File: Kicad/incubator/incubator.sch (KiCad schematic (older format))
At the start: 25 parts, among them J1 Barrel_Jack_MountingPin, J2 Conn_01x06, J3 Conn_01x01, J4 RJ12, J5 Conn_01x01, J6 Conn_01x01, J7 Conn_01x01, J8 Conn_02x03_Odd_Even, U1 LM78M05_TO252

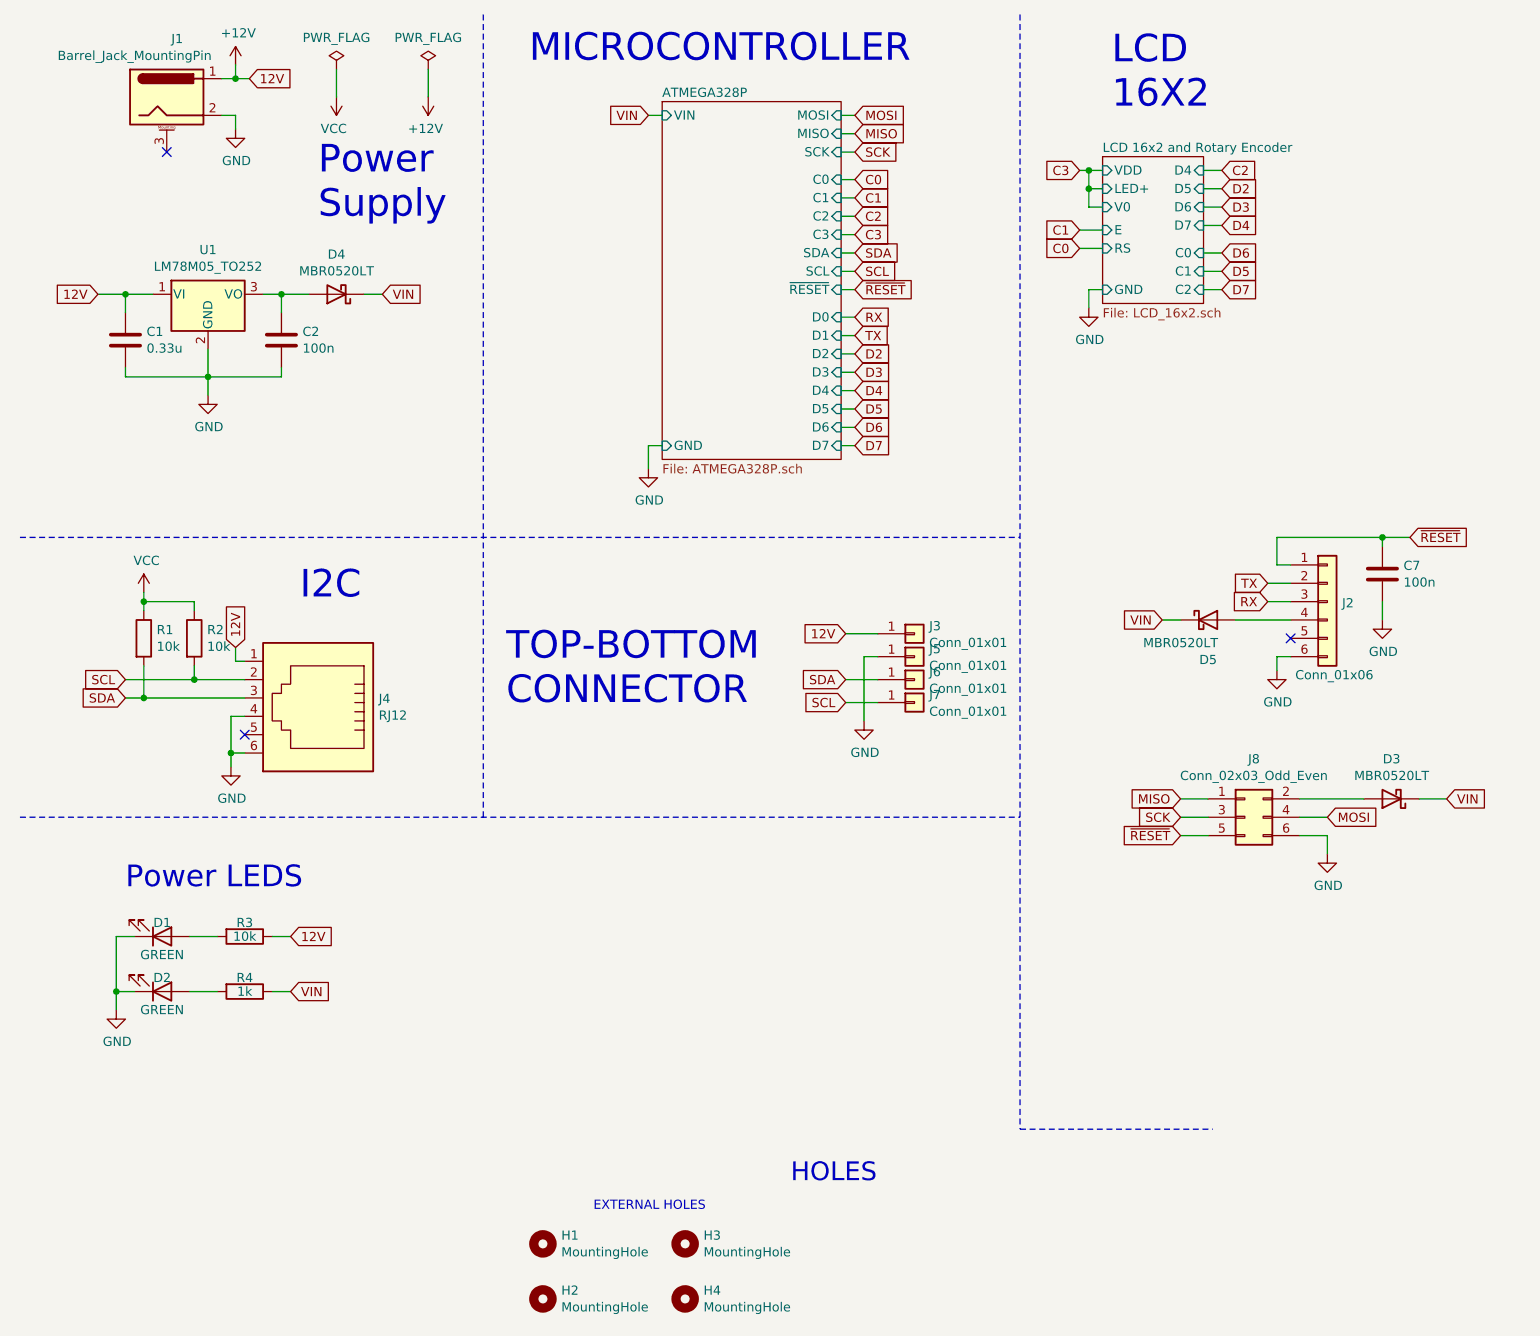
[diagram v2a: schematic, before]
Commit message: fix: iss #1: add ERROR and BLINKING LED, iss #2: solved
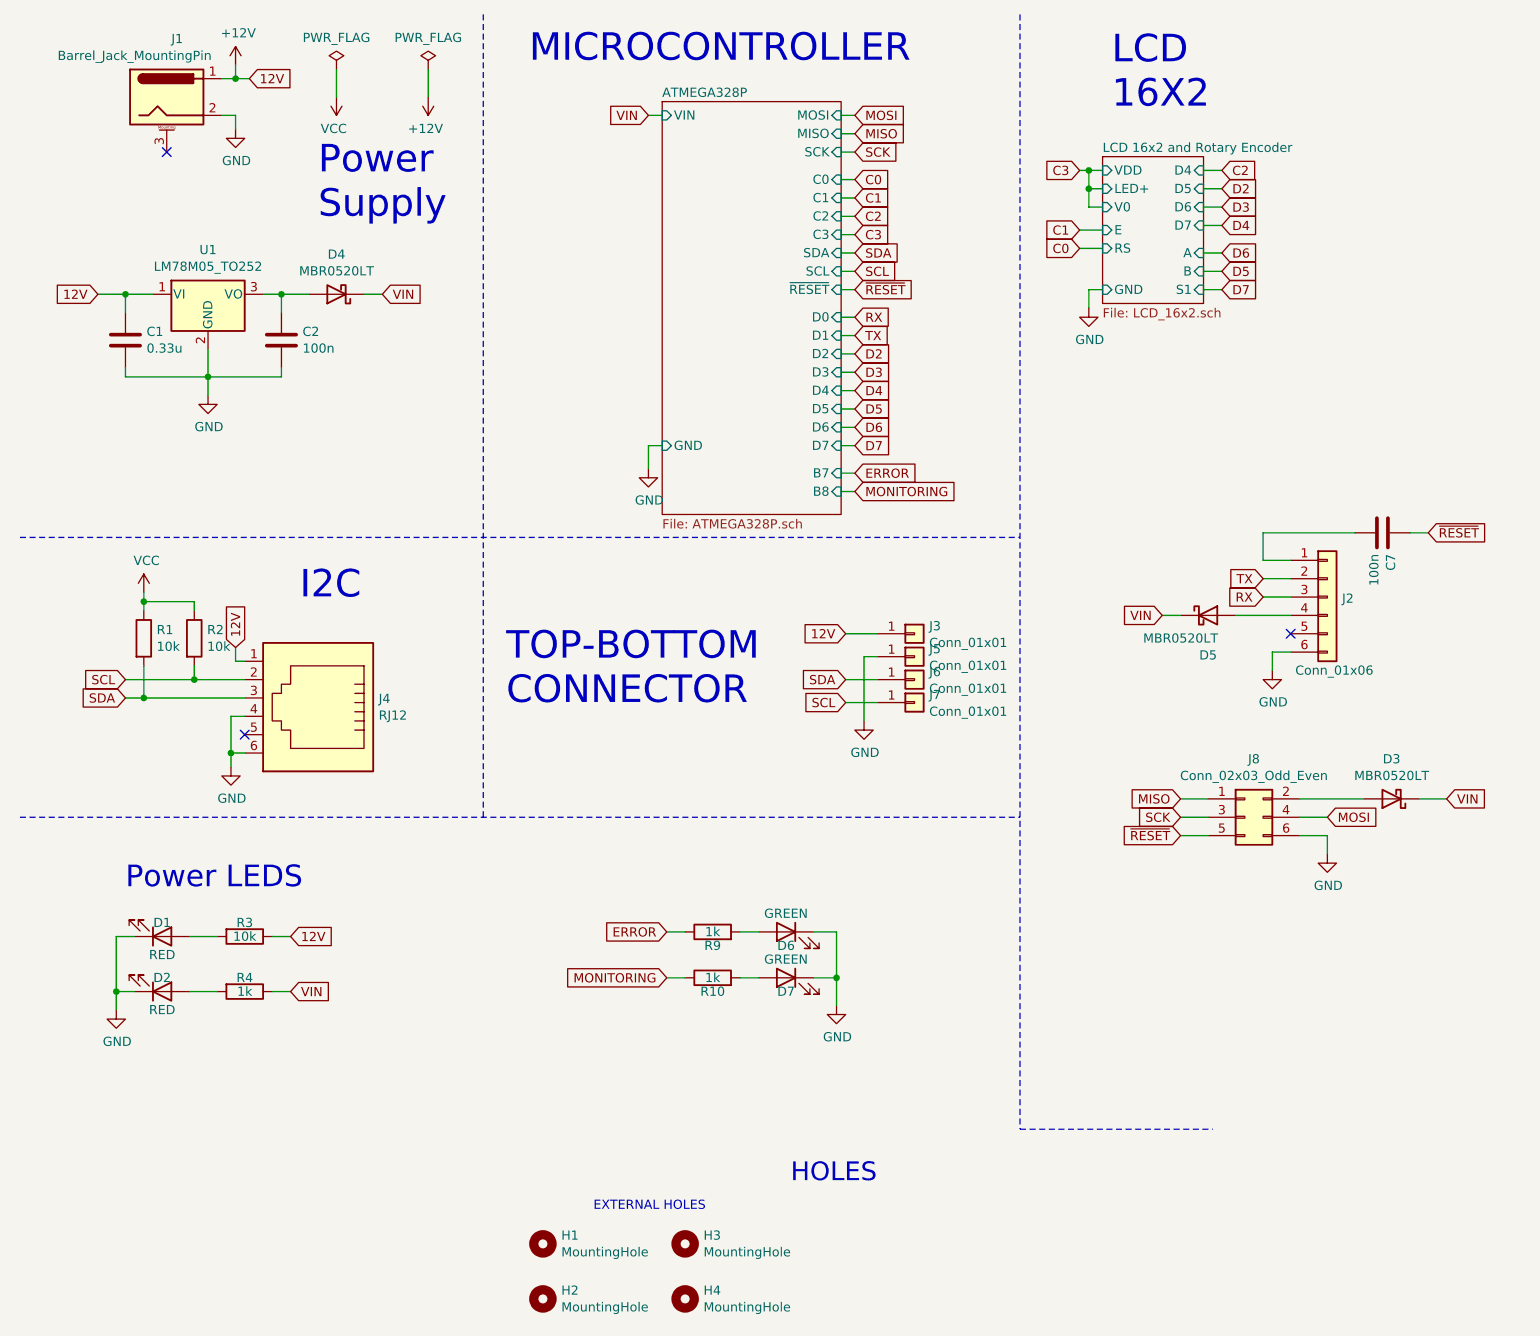
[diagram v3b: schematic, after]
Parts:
- added D6, D7: GREEN, LED_SMD:LED_0805_2012Metric_Pad1.15x1.40mm_HandSolder, symbol Device:LED
- added R10, R9: 1k, Resistor_SMD:R_0805_2012Metric_Pad1.20x1.40mm_HandSolder, symbol Device:R
- D1, D2: value GREEN -> RED
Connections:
- net GND: now also D6.1 (K), D7.1 (K); no longer C7.2
- net ~RESET: no longer J2.1 (Pin_1)
- new net: C7.2, J2.1 (Pin_1)
- new net: D7.2 (A), R10.2
- new net: D6.2 (A), R9.2
- new net ERROR: R9.1
- new net MONITORING: R10.1
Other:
- moved on the sheet: C7, D5, J2
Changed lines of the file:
@@
 Title "Incubator"
 Date "2021-07-26"
-Rev "0.1"
+Rev "0.2"
 Comp ""
 Comment1 ""
@@
 $EndComp
 $Sheet
-S 3975 950  975  1950
+S 3975 950  975  2250
 U 61116939
 F0 "ATMEGA328P" 50
@@
 F20 "MISO" I R 4950 1125 50
 F21 "SCK" I R 4950 1225 50
+F22 "B7" I R 4950 2975 50
+F23 "B8" I R 4950 3075 50
 $EndSheet
 Wire Wire Line
@@
 Wire Wire Line
 	3900 2825 3900 2950
-Text GLabel 6250 1325 0    50   Input ~ 0
-C3
-Text GLabel 6250 1650 0    50   Input ~ 0
-C1
-Text GLabel 6250 1750 0    50   Input ~ 0
-C0
-Text GLabel 7025 1325 2    50   Input ~ 0
-C2
-Text GLabel 7025 1425 2    50   Input ~ 0
-D2
-Text GLabel 7025 1525 2    50   Input ~ 0
-D3
-Text GLabel 7025 1625 2    50   Input ~ 0
-D4
-Text GLabel 7025 1775 2    50   Input ~ 0
-D6
-Text GLabel 7025 1875 2    50   Input ~ 0
-D5
-Text GLabel 7025 1975 2    50   Input ~ 0
-D7
 $Comp
 L incubator-rescue:GND-power #PWR0114
@@
 Wire Wire Line
 	6925 1525 7025 1525
-$Sheet
-S 6375 1250 550  800
-U 611AEB1E
-F0 "LCD 16x2 and Rotary Encoder" 50
-F1 "LCD_16x2.sch" 50
-F2 "D4" I R 6925 1325 50
-F3 "D5" I R 6925 1425 50
-F4 "D6" I R 6925 1525 50
-F5 "D7" I R 6925 1625 50
-F6 "GND" I L 6375 1975 50
-F7 "C0" I R 6925 1775 50
-F8 "C1" I R 6925 1875 50
-F9 "C2" I R 6925 1975 50
-F10 "E" I L 6375 1650 50
-F11 "RS" I L 6375 1750 50
-F12 "VDD" I L 6375 1325 50
-F13 "LED+" I L 6375 1425 50
-F14 "V0" I L 6375 1525 50
-$EndSheet
 Wire Wire Line
 	6925 1775 7025 1775
@@
 	1    0    0    -1
 $EndComp
-$Comp
-L incubator-rescue:Conn_01x06-Connector_Generic J2
-U 1 1 610D151B
-P 7600 3675
-F 0 "J2" H 7680 3667 50  0000 L CNN
-F 1 "Conn_01x06" H 7425 3275 50  0000 L CNN
-F 2 "Connector_PinHeader_2.54mm:PinHeader_1x06_P2.54mm_Vertical" H 7600 3675 50  0001 C CNN
-F 3 "~" H 7600 3675 50  0001 C CNN
-	1    7600 3675
-	1    0    0    -1
-$EndComp
 Text GLabel 2450 2000 2    50   Input ~ 0
 VIN
-Text GLabel 8050 3325 2    50   Input ~ 0
+Text GLabel 8150 3300 2    50   Input ~ 0
 ~RESET
-Text GLabel 7275 3575 0    50   Input ~ 0
+Text GLabel 7250 3550 0    50   Input ~ 0
 TX
 $Comp
 L incubator-rescue:GND-power #PWR0103
 U 1 1 610EBE3F
-P 7325 4050
-F 0 "#PWR0103" H 7325 3800 50  0001 C CNN
-F 1 "GND" H 7330 3877 50  0000 C CNN
-F 2 "" H 7325 4050 50  0001 C CNN
-F 3 "" H 7325 4050 50  0001 C CNN
-	1    7325 4050
-	1    0    0    -1
-$EndComp
-Wire Wire Line
-	7400 3575 7275 3575
-Wire Wire Line
-	7275 3675 7400 3675
-Wire Wire Line
-	7400 3975 7325 3975
-Wire Wire Line
-	7325 3975 7325 4050
-Text GLabel 7275 3675 0    50   Input ~ 0
+P 7300 4050
+F 0 "#PWR0103" H 7300 3800 50  0001 C CNN
+F 1 "GND" H 7305 3877 50  0000 C CNN
+F 2 "" H 7300 4050 50  0001 C CNN
+F 3 "" H 7300 4050 50  0001 C CNN
+	1    7300 4050
+	1    0    0    -1
+$EndComp
+Text GLabel 7250 3650 0    50   Input ~ 0
 RX
 $Comp
@@
 L incubator-rescue:C-Device C?
 U 1 1 61154027
-P 7900 3525
+P 7900 3300
 AR Path="/61116939/61154027" Ref="C?"  Part="1"
 AR Path="/61154027" Ref="C7"  Part="1"
-F 0 "C7" H 8015 3571 50  0000 L CNN
-F 1 "100n" H 8015 3480 50  0000 L CNN
-F 2 "Capacitor_SMD:C_0805_2012Metric_Pad1.18x1.45mm_HandSolder" H 7938 3375 50  0001 C CNN
-F 3 "~" H 7900 3525 50  0001 C CNN
-	1    7900 3525
-	1    0    0    -1
-$EndComp
-Wire Wire Line
-	7100 3775 7400 3775
-Wire Wire Line
-	6800 3775 6700 3775
-Text GLabel 6700 3775 0    50   Input ~ 0
+F 0 "C7" H 8015 3346 50  0000 L CNN
+F 1 "100n" H 8015 3255 50  0000 L CNN
+F 2 "Capacitor_SMD:C_0805_2012Metric_Pad1.18x1.45mm_HandSolder" H 7938 3150 50  0001 C CNN
+F 3 "~" H 7900 3300 50  0001 C CNN
+	1    7900 3300
+	0    1    1    0
+$EndComp
+Text GLabel 6700 3750 0    50   Input ~ 0
 VIN
-Wire Wire Line
-	7400 3475 7325 3475
-Wire Wire Line
-	7325 3475 7325 3325
-Wire Wire Line
-	7325 3325 7900 3325
-$Comp
-L incubator-rescue:GND-power #PWR0106
-U 1 1 6117A969
-P 7900 3775
-F 0 "#PWR0106" H 7900 3525 50  0001 C CNN
-F 1 "GND" H 7905 3602 50  0000 C CNN
-F 2 "" H 7900 3775 50  0001 C CNN
-F 3 "" H 7900 3775 50  0001 C CNN
-	1    7900 3775
-	1    0    0    -1
-$EndComp
-Wire Wire Line
-	7900 3775 7900 3675
-Wire Wire Line
-	7900 3375 7900 3325
-Connection ~ 7900 3325
-Wire Wire Line
-	7900 3325 8050 3325
 Text GLabel 1725 825  2    50   Input ~ 0
 12V
@@
 L incubator-rescue:MBR0520LT-Diode D5
 U 1 1 61109529
-P 6950 3775
-F 0 "D5" H 6950 3558 50  0000 C CNN
-F 1 "MBR0520LT" H 6800 3650 50  0000 C CNN
-F 2 "Diode_SMD:D_SOD-123" H 6950 3600 50  0001 C CNN
-F 3 "http://www.onsemi.com/pub_link/Collateral/MBR0520LT1-D.PDF" H 6950 3775 50  0001 C CNN
-	1    6950 3775
-	1    0    0    -1
-$EndComp
-NoConn ~ 7400 3875
+P 6950 3750
+F 0 "D5" H 6950 3533 50  0000 C CNN
+F 1 "MBR0520LT" H 6800 3625 50  0000 C CNN
+F 2 "Diode_SMD:D_SOD-123" H 6950 3575 50  0001 C CNN
+F 3 "http://www.onsemi.com/pub_link/Collateral/MBR0520LT1-D.PDF" H 6950 3750 50  0001 C CNN
+	1    6950 3750
+	1    0    0    -1
+$EndComp
 $Comp
 L incubator-rescue:Conn_01x01-Connector_Generic J3
@@
 AR Path="/614D57B2" Ref="D1"  Part="1"
 F 0 "D1" H 1250 5425 50  0000 C CNN
-F 1 "GREEN" H 1250 5600 50  0000 C CNN
+F 1 "RED" H 1250 5600 50  0000 C CNN
 F 2 "LED_SMD:LED_0805_2012Metric_Pad1.15x1.40mm_HandSolder" H 1250 5500 50  0001 C CNN
 F 3 "~" H 1250 5500 50  0001 C CNN
@@
 AR Path="/614D57B8" Ref="D2"  Part="1"
 F 0 "D2" H 1250 5725 50  0000 C CNN
-F 1 "GREEN" H 1250 5900 50  0000 C CNN
+F 1 "RED" H 1250 5900 50  0000 C CNN
 F 2 "LED_SMD:LED_0805_2012Metric_Pad1.15x1.40mm_HandSolder" H 1250 5800 50  0001 C CNN
 F 3 "~" H 1250 5800 50  0001 C CNN
@@
 Wire Wire Line
 	6800 4950 6950 4950
+$Comp
+L incubator-rescue:Conn_01x06-Connector_Generic J2
+U 1 1 610D151B
+P 7600 3650
+F 0 "J2" H 7680 3642 50  0000 L CNN
+F 1 "Conn_01x06" H 7425 3250 50  0000 L CNN
+F 2 "Connector_PinHeader_2.54mm:PinHeader_1x06_P2.54mm_Vertical" H 7600 3650 50  0001 C CNN
+F 3 "~" H 7600 3650 50  0001 C CNN
+	1    7600 3650
+	1    0    0    -1
+$EndComp
+Wire Wire Line
+	7750 3300 7250 3300
+Wire Wire Line
+	7250 3300 7250 3450
+Wire Wire Line
+	7250 3450 7400 3450
+Wire Wire Line
+	8050 3300 8150 3300
+Wire Wire Line
+	6700 3750 6800 3750
+Wire Wire Line
+	7100 3750 7400 3750
+NoConn ~ 7400 3850
+Wire Wire Line
+	7400 3950 7300 3950
+Wire Wire Line
+	7300 3950 7300 4050
+Wire Wire Line
+	7250 3650 7400 3650
+Wire Wire Line
+	7400 3550 7250 3550
+Text GLabel 6250 1750 0    50   Input ~ 0
+C0
+Text GLabel 6250 1650 0    50   Input ~ 0
+C1
+Text GLabel 6250 1325 0    50   Input ~ 0
+C3
+Text GLabel 7025 1625 2    50   Input ~ 0
+D4
+Text GLabel 7025 1525 2    50   Input ~ 0
+D3
+Text GLabel 7025 1425 2    50   Input ~ 0
+D2
+Text GLabel 7025 1325 2    50   Input ~ 0
+C2
+Text GLabel 7025 1975 2    50   Input ~ 0
+D7
+Text GLabel 7025 1875 2    50   Input ~ 0
+D5
+Text GLabel 7025 1775 2    50   Input ~ 0
+D6
+$Sheet
+S 6375 1250 550  800
+U 611AEB1E
+F0 "LCD 16x2 and Rotary Encoder" 50
+F1 "LCD_16x2.sch" 50
+F2 "D4" I R 6925 1325 50
+F3 "D5" I R 6925 1425 50
+F4 "D6" I R 6925 1525 50
+F5 "D7" I R 6925 1625 50
+F6 "GND" I L 6375 1975 50
+F7 "A" I R 6925 1775 50
+F8 "B" I R 6925 1875 50
+F9 "S1" I R 6925 1975 50
+F10 "E" I L 6375 1650 50
+F11 "RS" I L 6375 1750 50
+F12 "VDD" I L 6375 1325 50
+F13 "LED+" I L 6375 1425 50
+F14 "V0" I L 6375 1525 50
+$EndSheet
+$Comp
+L Device:R R?
+U 1 1 6193BEE6
+P 4250 5725
+AR Path="/5E0D7B92/6193BEE6" Ref="R?"  Part="1"
+AR Path="/5E0D7D04/6193BEE6" Ref="R?"  Part="1"
+AR Path="/6193BEE6" Ref="R10"  Part="1"
+AR Path="/5E0005EE/6193BEE6" Ref="R?"  Part="1"
+AR Path="/614262A1/6193BEE6" Ref="R?"  Part="1"
+F 0 "R10" V 4175 5725 50  0000 C CNN
+F 1 "1k" V 4250 5725 50  0000 C CNN
+F 2 "Resistor_SMD:R_0805_2012Metric_Pad1.20x1.40mm_HandSolder" V 4180 5725 50  0001 C CNN
+F 3 "~" H 4250 5725 50  0001 C CNN
+	1    4250 5725
+	0    -1   -1   0
+$EndComp
+$Comp
+L Device:LED D?
+U 1 1 6193C98D
+P 4650 5725
+AR Path="/614262A1/6193C98D" Ref="D?"  Part="1"
+AR Path="/6193C98D" Ref="D7"  Part="1"
+F 0 "D7" H 4650 5650 50  0000 C CNN
+F 1 "GREEN" H 4650 5825 50  0000 C CNN
+F 2 "LED_SMD:LED_0805_2012Metric_Pad1.15x1.40mm_HandSolder" H 4650 5725 50  0001 C CNN
+F 3 "~" H 4650 5725 50  0001 C CNN
+	1    4650 5725
+	-1   0    0    -1
+$EndComp
+$Comp
+L Device:R R?
+U 1 1 6193CDAE
+P 4250 5475
+AR Path="/5E0D7B92/6193CDAE" Ref="R?"  Part="1"
+AR Path="/5E0D7D04/6193CDAE" Ref="R?"  Part="1"
+AR Path="/6193CDAE" Ref="R9"  Part="1"
+AR Path="/5E0005EE/6193CDAE" Ref="R?"  Part="1"
+AR Path="/614262A1/6193CDAE" Ref="R?"  Part="1"
+F 0 "R9" V 4175 5475 50  0000 C CNN
+F 1 "1k" V 4250 5475 50  0000 C CNN
+F 2 "Resistor_SMD:R_0805_2012Metric_Pad1.20x1.40mm_HandSolder" V 4180 5475 50  0001 C CNN
+F 3 "~" H 4250 5475 50  0001 C CNN
+	1    4250 5475
+	0    -1   -1   0
+$EndComp
+$Comp
+L Device:LED D?
+U 1 1 6193D088
+P 4650 5475
+AR Path="/614262A1/6193D088" Ref="D?"  Part="1"
+AR Path="/6193D088" Ref="D6"  Part="1"
+F 0 "D6" H 4650 5400 50  0000 C CNN
+F 1 "GREEN" H 4650 5575 50  0000 C CNN
+F 2 "LED_SMD:LED_0805_2012Metric_Pad1.15x1.40mm_HandSolder" H 4650 5475 50  0001 C CNN
+F 3 "~" H 4650 5475 50  0001 C CNN
+	1    4650 5475
+	-1   0    0    -1
+$EndComp
+Text GLabel 5025 2975 2    50   Input ~ 0
+ERROR
+Text GLabel 5025 3075 2    50   Input ~ 0
+MONITORING
+Wire Wire Line
+	4950 2975 5025 2975
+Wire Wire Line
+	5025 3075 4950 3075
+Text GLabel 4000 5475 0    50   Input ~ 0
+ERROR
+Text GLabel 4000 5725 0    50   Input ~ 0
+MONITORING
+Wire Wire Line
+	4100 5725 4000 5725
+Wire Wire Line
+	4400 5725 4500 5725
+$Comp
+L incubator-rescue:GND-power #PWR0106
+U 1 1 6196DBDC
+P 4925 5875
+F 0 "#PWR0106" H 4925 5625 50  0001 C CNN
+F 1 "GND" H 4930 5702 50  0000 C CNN
+F 2 "" H 4925 5875 50  0001 C CNN
+F 3 "" H 4925 5875 50  0001 C CNN
+	1    4925 5875
+	1    0    0    -1
+$EndComp
+Wire Wire Line
+	4800 5725 4925 5725
+Connection ~ 4925 5725
+Wire Wire Line
+	4925 5725 4925 5875
+Wire Wire Line
+	4000 5475 4100 5475
+Wire Wire Line
+	4400 5475 4500 5475
+Wire Wire Line
+	4800 5475 4925 5475
+Wire Wire Line
+	4925 5475 4925 5725
 $EndSCHEMATC
